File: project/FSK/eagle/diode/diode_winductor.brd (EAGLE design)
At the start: 100 x 80 mm, 10 parts, among them X1 SMA-142-0701-801/806, X2 SMA-142-0701-801/806

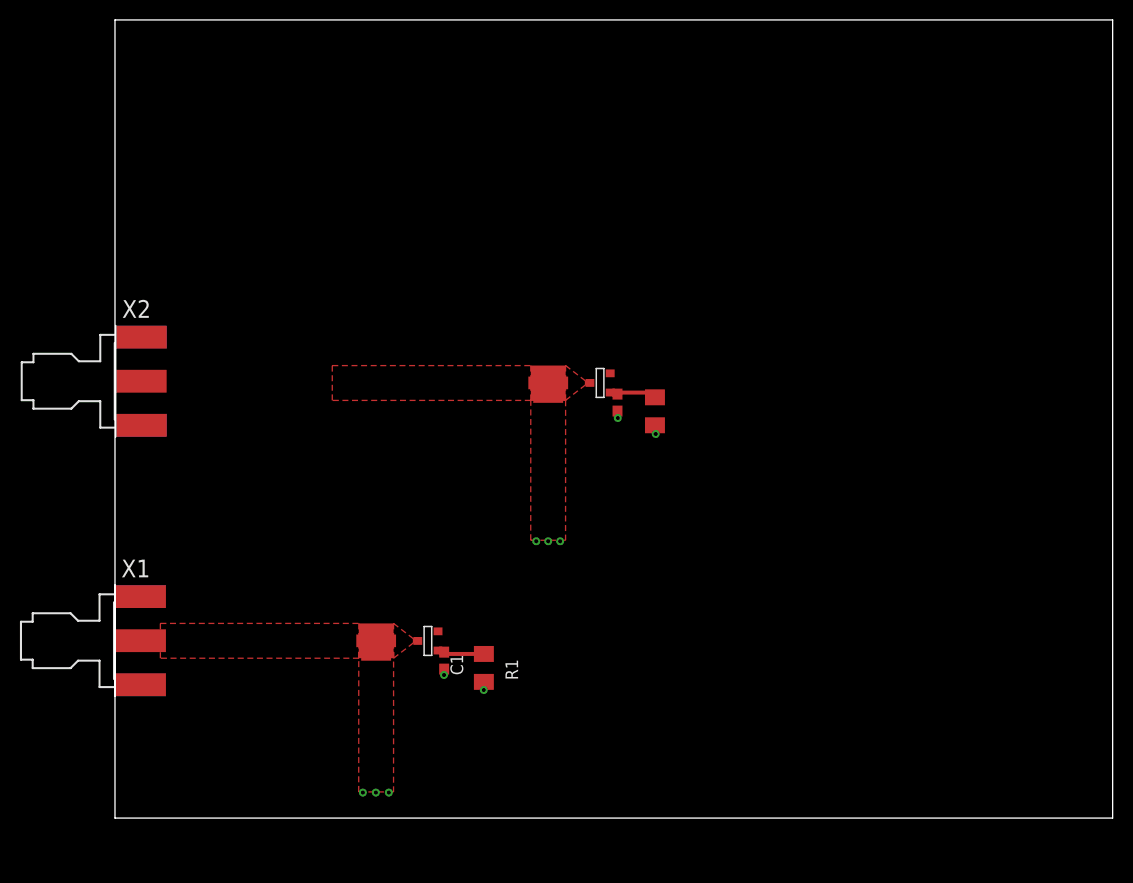
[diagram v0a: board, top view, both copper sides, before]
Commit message: added diode with inductor matching
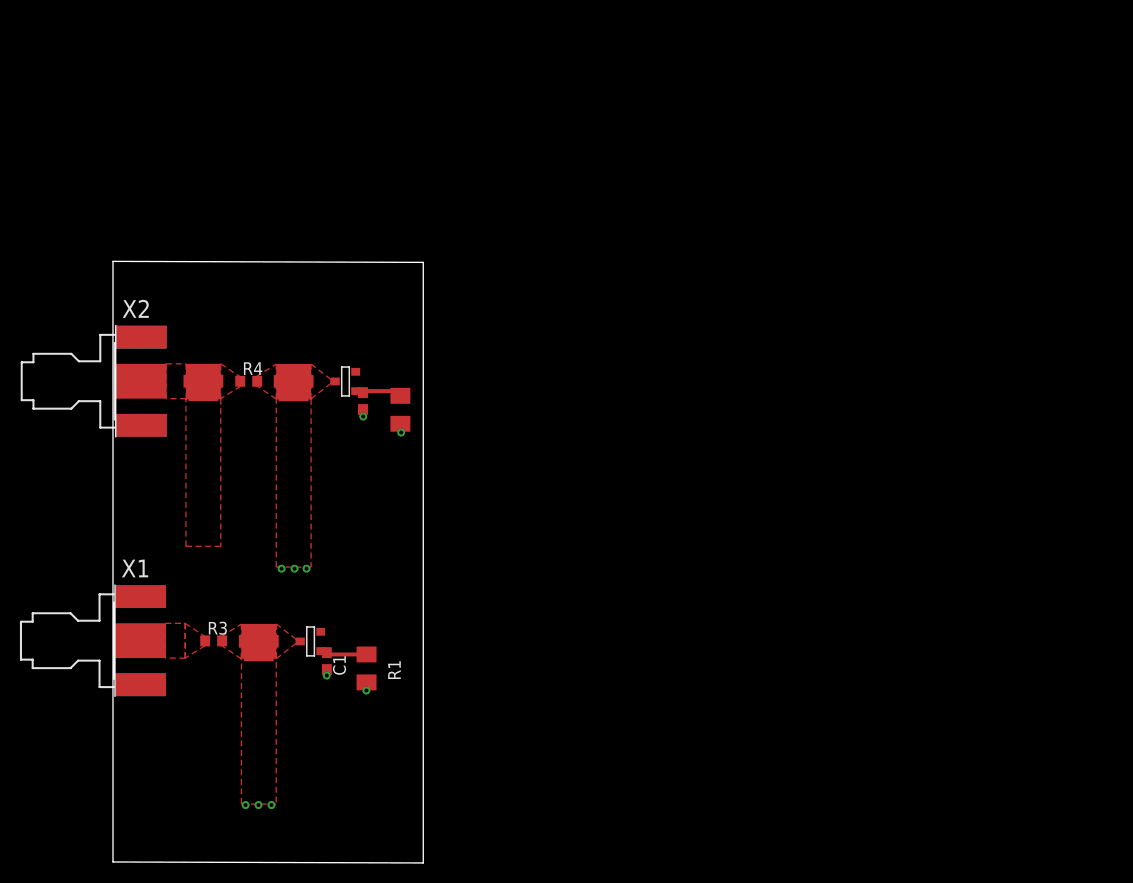
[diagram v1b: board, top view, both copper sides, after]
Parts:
- added INPUT2: TEE_TL1, ECE532_Parts:TEE_TL1
- added R3, R4: (no value), rcl:R0603
- moved C2 25.5 mm to (24.9, 41.8)
- moved R2 25.5 mm to (28.6, 40.9)
- moved INPUT1 25.5 mm to (17.9, 42.5)
- moved U$2 25.5 mm to (23.1, 43.8)
- moved C1 11.8 mm to (21.2, 15.7)
- moved INPUT 11.8 mm to (14.4, 16.4)
- moved R1 11.8 mm to (25.2, 15.0)
- moved U$1 11.8 mm to (19.6, 17.7)
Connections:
- new net INPUT11: R3.1, X1.1
- new net INPUT2: INPUT1.T_B, INPUT1.T_L, INPUT1.T_R, R4.2, U$2.A
- net INPUT: now also R3.2; no longer X1.1
- net INPUT1: now also INPUT2.T_B, INPUT2.T_L, INPUT2.T_R, R4.1; no longer INPUT1.T_B, INPUT1.T_L, INPUT1.T_R, U$2.A
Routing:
- added copper zone on layer 1, net INPUT11
- added copper zone on layer 1, net INPUT2
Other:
- board size 100 x 80 mm -> 31.1 x 60.3 mm
